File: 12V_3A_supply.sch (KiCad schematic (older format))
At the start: 14 parts, among them U1 TPS54561

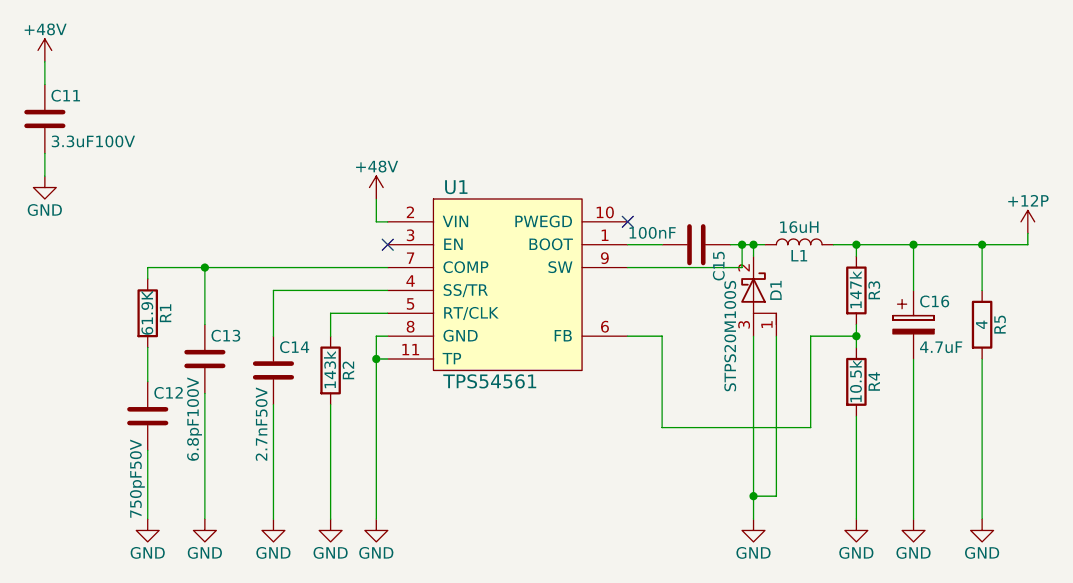
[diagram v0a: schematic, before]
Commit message: add MPN and change footprints
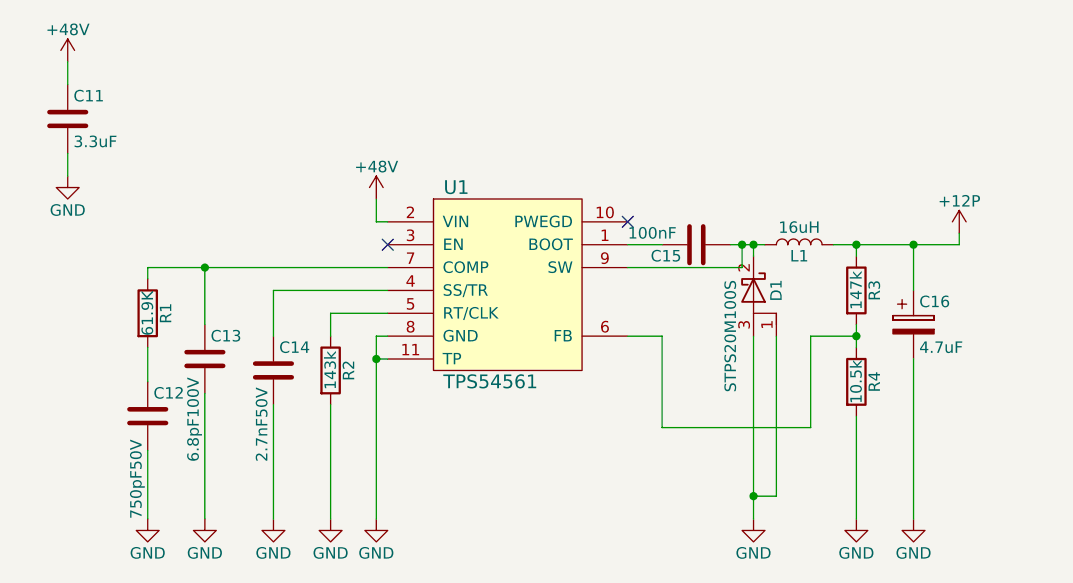
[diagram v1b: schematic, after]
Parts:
- removed R5: 4, Resistors_SMD:R_0402, symbol R
- C11: value 3.3uF100V -> 3.3uF; footprint Capacitors_SMD:C_1206 -> Capacitors_SMD:C_1210; MPN (none) -> 2211157
- C12: MPN (none) -> 1865436
- C13: MPN (none) -> 1865503
- C14: footprint Capacitors_SMD:C_0805 -> Capacitors_SMD:C_0603; MPN (none) -> 2680086
- C15: MPN (none) -> 2690952
- C16: footprint (none) -> Capacitor_SMD:CP_Elec_4x5.3; MPN (none) -> 2630483
- D1: MPN (none) -> 2325907
- L1: MPN (none) -> 2211625
- R1: MPN (none) -> 2073167
- R2: MPN (none) -> 2140944
- R3: MPN (none) -> 2302855
- R4: MPN (none) -> 1803138
- U1: MPN (none) -> TPS54561DPRT
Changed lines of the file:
@@
 LIBS:contrib
 LIBS:valves
+LIBS:MB_DEVICE
 LIBS:power_board-cache
 EELAYER 25 0
@@
 F 2 "MB_LIB:TPS54561" H 5450 3400 60  0001 C CNN
 F 3 "" H 5450 3400 60  0001 C CNN
+F 4 "TPS54561DPRT" H 5450 3400 60  0001 C CNN "MPN"
 	1    5450 3400
 	1    0    0    -1
@@
 Connection ~ 4900 3650
 $Comp
-L GND #PWR023
+L GND #PWR033
 U 1 1 5AA6E74F
 P 4900 4350
-F 0 "#PWR023" H 4900 4100 50  0001 C CNN
+F 0 "#PWR033" H 4900 4100 50  0001 C CNN
 F 1 "GND" H 4900 4200 50  0000 C CNN
 F 2 "" H 4900 4350 50  0001 C CNN
 F 3 "" H 4900 4350 50  0001 C CNN
 	1    4900 4350
-	1    0    0    -1
-$EndComp
-$Comp
-L C C11
-U 1 1 5AA6E768
-P 3450 2600
-F 0 "C11" H 3475 2700 50  0000 L CNN
-F 1 "3.3uF100V" H 3475 2500 50  0000 L CNN
-F 2 "Capacitors_SMD:C_1206" H 3488 2450 50  0001 C CNN
-F 3 "" H 3450 2600 50  0001 C CNN
-	1    3450 2600
 	1    0    0    -1
 $EndComp
@@
 F 2 "Capacitors_SMD:C_0402" H 3938 3750 50  0001 C CNN
 F 3 "" H 3900 3900 50  0001 C CNN
+F 4 "1865436" H 3900 3900 60  0001 C CNN "MPN"
 	1    3900 3900
-	1    0    0    -1
-$EndComp
-$Comp
-L C C13
-U 1 1 5AA6E7C6
-P 4150 3650
-F 0 "C13" H 4175 3750 50  0000 L CNN
-F 1 "6.8pF100V" V 4100 3200 50  0000 L CNN
-F 2 "Capacitors_SMD:C_0603" H 4188 3500 50  0001 C CNN
-F 3 "" H 4150 3650 50  0001 C CNN
-	1    4150 3650
-	1    0    0    -1
-$EndComp
-$Comp
-L C C14
-U 1 1 5AA6E7E8
-P 4450 3700
-F 0 "C14" H 4475 3800 50  0000 L CNN
-F 1 "2.7nF50V" V 4400 3300 50  0000 L CNN
-F 2 "Capacitors_SMD:C_0805" H 4488 3550 50  0001 C CNN
-F 3 "" H 4450 3700 50  0001 C CNN
-	1    4450 3700
 	1    0    0    -1
 $EndComp
@@
 F 2 "Resistors_SMD:R_0402" V 3830 3450 50  0001 C CNN
 F 3 "" H 3900 3450 50  0001 C CNN
+F 4 "2073167" V 3900 3450 60  0001 C CNN "MPN"
 	1    3900 3450
 	1    0    0    -1
@@
 F 2 "Resistors_SMD:R_0402" V 4630 3700 50  0001 C CNN
 F 3 "" H 4700 3700 50  0001 C CNN
+F 4 "2140944" V 4700 3700 60  0001 C CNN "MPN"
 	1    4700 3700
 	1    0    0    -1
-$EndComp
-$Comp
-L C C15
-U 1 1 5AA6E89F
-P 6300 3150
-F 0 "C15" H 6325 3250 50  0000 L CNN
-F 1 "100nF" V 6250 2850 50  0000 L CNN
-F 2 "Capacitors_SMD:C_0402" H 6338 3000 50  0001 C CNN
-F 3 "" H 6300 3150 50  0001 C CNN
-	1    6300 3150
-	0    1    1    0
 $EndComp
 $Comp
@@
 F 2 "Resistors_SMD:R_0402" V 6930 3350 50  0001 C CNN
 F 3 "" H 7000 3350 50  0001 C CNN
+F 4 "2302855" V 7000 3350 60  0001 C CNN "MPN"
 	1    7000 3350
 	1    0    0    -1
@@
 F 2 "Resistors_SMD:R_0402" V 6930 3750 50  0001 C CNN
 F 3 "" H 7000 3750 50  0001 C CNN
+F 4 "1803138" V 7000 3750 60  0001 C CNN "MPN"
 	1    7000 3750
 	1    0    0    -1
 $EndComp
 $Comp
-L +48V #PWR024
-U 1 1 5AA6EAEE
-P 3450 2350
-F 0 "#PWR024" H 3450 2200 50  0001 C CNN
-F 1 "+48V" H 3450 2490 50  0000 C CNN
-F 2 "" H 3450 2350 50  0001 C CNN
-F 3 "" H 3450 2350 50  0001 C CNN
-	1    3450 2350
-	1    0    0    -1
-$EndComp
-$Comp
-L +48V #PWR025
+L +48V #PWR034
 U 1 1 5AA6EB2F
 P 4900 2950
-F 0 "#PWR025" H 4900 2800 50  0001 C CNN
+F 0 "#PWR034" H 4900 2800 50  0001 C CNN
 F 1 "+48V" H 4900 3090 50  0000 C CNN
 F 2 "" H 4900 2950 50  0001 C CNN
@@
 	1    0    0    -1
 $EndComp
-$Comp
-L GND #PWR026
-U 1 1 5AA6EB62
-P 3450 2850
-F 0 "#PWR026" H 3450 2600 50  0001 C CNN
-F 1 "GND" H 3450 2700 50  0000 C CNN
-F 2 "" H 3450 2850 50  0001 C CNN
-F 3 "" H 3450 2850 50  0001 C CNN
-	1    3450 2850
-	1    0    0    -1
-$EndComp
 Wire Wire Line
 	4900 2950 4900 3050
 Wire Wire Line
 	4900 3050 4950 3050
-Wire Wire Line
-	3450 2850 3450 2750
-Wire Wire Line
-	3450 2450 3450 2350
 Wire Wire Line
 	4150 3500 4150 3250
@@
 	3900 4050 3900 4350
 Wire Wire Line
-	4150 3800 4150 4350
-Wire Wire Line
 	4450 3850 4450 4350
 Wire Wire Line
 	4700 3850 4700 4350
 $Comp
-L GND #PWR027
+L GND #PWR035
 U 1 1 5AA6EECF
 P 4700 4350
-F 0 "#PWR027" H 4700 4100 50  0001 C CNN
+F 0 "#PWR035" H 4700 4100 50  0001 C CNN
 F 1 "GND" H 4700 4200 50  0000 C CNN
 F 2 "" H 4700 4350 50  0001 C CNN
@@
 $EndComp
 $Comp
-L GND #PWR028
+L GND #PWR036
 U 1 1 5AA6EEF8
 P 4450 4350
-F 0 "#PWR028" H 4450 4100 50  0001 C CNN
+F 0 "#PWR036" H 4450 4100 50  0001 C CNN
 F 1 "GND" H 4450 4200 50  0000 C CNN
 F 2 "" H 4450 4350 50  0001 C CNN
@@
 $EndComp
 $Comp
-L GND #PWR029
+L GND #PWR037
 U 1 1 5AA6EF21
 P 4150 4350
-F 0 "#PWR029" H 4150 4100 50  0001 C CNN
+F 0 "#PWR037" H 4150 4100 50  0001 C CNN
 F 1 "GND" H 4150 4200 50  0000 C CNN
 F 2 "" H 4150 4350 50  0001 C CNN
@@
 $EndComp
 $Comp
-L GND #PWR030
+L GND #PWR038
 U 1 1 5AA6EF4A
 P 3900 4350
-F 0 "#PWR030" H 3900 4100 50  0001 C CNN
+F 0 "#PWR038" H 3900 4100 50  0001 C CNN
 F 1 "GND" H 3900 4200 50  0000 C CNN
 F 2 "" H 3900 4350 50  0001 C CNN
@@
 F 2 "Inductors_SMD:L_Wuerth_HCI-1050" H 6750 3150 50  0001 C CNN
 F 3 "http://katalog.we-online.de/pbs/datasheet/7443251600.pdf" H 6750 3150 50  0001 C CNN
+F 4 "2211625" V 6750 3150 60  0001 C CNN "MPN"
 	1    6750 3150
 	0    -1   -1   0
@@
 F 0 "C16" H 7275 3600 50  0000 L CNN
 F 1 "4.7uF" H 7275 3400 50  0000 L CNN
-F 2 "" H 7288 3350 50  0001 C CNN
+F 2 "Capacitor_SMD:CP_Elec_4x5.3" H 7288 3350 50  0001 C CNN
 F 3 "" H 7250 3500 50  0001 C CNN
+F 4 "2630483" H 7250 3500 60  0001 C CNN "MPN"
 	1    7250 3500
 	1    0    0    -1
@@
 Connection ~ 7000 3150
 Wire Wire Line
-	6900 3150 7750 3150
+	6900 3150 7450 3150
 Wire Wire Line
 	7250 3150 7250 3350
 Wire Wire Line
 	7250 3650 7250 4350
-$Comp
-L R R5
-U 1 1 5AA6F613
-P 7550 3500
-F 0 "R5" V 7630 3500 50  0000 C CNN
-F 1 "4" V 7550 3500 50  0000 C CNN
-F 2 "Resistors_SMD:R_0402" V 7480 3500 50  0001 C CNN
-F 3 "" H 7550 3500 50  0001 C CNN
-	1    7550 3500
-	1    0    0    -1
-$EndComp
-Wire Wire Line
-	7550 3150 7550 3350
 Connection ~ 7250 3150
-Wire Wire Line
-	7550 3650 7550 4350
 Wire Wire Line
 	6000 3250 6500 3250
@@
 Connection ~ 6550 3150
 $Comp
-L GND #PWR031
+L GND #PWR039
 U 1 1 5AA6F863
 P 6550 4350
-F 0 "#PWR031" H 6550 4100 50  0001 C CNN
+F 0 "#PWR039" H 6550 4100 50  0001 C CNN
 F 1 "GND" H 6550 4200 50  0000 C CNN
 F 2 "" H 6550 4350 50  0001 C CNN
@@
 	7000 3900 7000 4350
 $Comp
-L GND #PWR032
+L GND #PWR040
 U 1 1 5AA6F9CD
 P 7000 4350
-F 0 "#PWR032" H 7000 4100 50  0001 C CNN
+F 0 "#PWR040" H 7000 4100 50  0001 C CNN
 F 1 "GND" H 7000 4200 50  0000 C CNN
 F 2 "" H 7000 4350 50  0001 C CNN
@@
 $EndComp
 $Comp
-L GND #PWR033
+L GND #PWR041
 U 1 1 5AA6FA05
 P 7250 4350
-F 0 "#PWR033" H 7250 4100 50  0001 C CNN
+F 0 "#PWR041" H 7250 4100 50  0001 C CNN
 F 1 "GND" H 7250 4200 50  0000 C CNN
 F 2 "" H 7250 4350 50  0001 C CNN
@@
 	1    0    0    -1
 $EndComp
-$Comp
-L GND #PWR034
-U 1 1 5AA6FA3D
-P 7550 4350
-F 0 "#PWR034" H 7550 4100 50  0001 C CNN
-F 1 "GND" H 7550 4200 50  0000 C CNN
-F 2 "" H 7550 4350 50  0001 C CNN
-F 3 "" H 7550 4350 50  0001 C CNN
-	1    7550 4350
-	1    0    0    -1
-$EndComp
-Wire Wire Line
-	7750 3150 7750 3100
-Connection ~ 7550 3150
+Wire Wire Line
+	7450 3150 7450 3100
 $Comp
 L D_Schottky_AKA D1
@@
 F 2 "TO_SOT_Packages_SMD:TO-263-2" H 6550 3350 50  0001 C CNN
 F 3 "http://www.st.com/content/ccc/resource/technical/document/datasheet/group2/8f/d3/41/ea/82/b2/4b/5a/CD00228904/files/CD00228904.pdf/jcr:content/translations/en.CD00228904.pdf" H 6550 3350 50  0001 C CNN
+F 4 "2325907" H 6550 3350 60  0001 C CNN "MPN"
 	1    6550 3350
 	0    1    1    0
@@
 NoConn ~ 6000 3050
 $Comp
-L +12P #PWR035
+L +12P #PWR042
 U 1 1 5AA81E40
-P 7750 3100
-F 0 "#PWR035" H 7750 2950 50  0001 C CNN
-F 1 "+12P" H 7750 3240 50  0000 C CNN
-F 2 "" H 7750 3100 50  0001 C CNN
-F 3 "" H 7750 3100 50  0001 C CNN
-	1    7750 3100
-	1    0    0    -1
-$EndComp
+P 7450 3100
+F 0 "#PWR042" H 7450 2950 50  0001 C CNN
+F 1 "+12P" H 7450 3240 50  0000 C CNN
+F 2 "" H 7450 3100 50  0001 C CNN
+F 3 "" H 7450 3100 50  0001 C CNN
+	1    7450 3100
+	1    0    0    -1
+$EndComp
+$Comp
+L C C11
+U 1 1 5AB03638
+P 3550 2600
+F 0 "C11" H 3575 2700 50  0000 L CNN
+F 1 "3.3uF" H 3575 2500 50  0000 L CNN
+F 2 "Capacitors_SMD:C_1210" H 3588 2450 50  0001 C CNN
+F 3 "" H 3550 2600 50  0001 C CNN
+F 4 "2211157" H 3550 2600 60  0001 C CNN "MPN"
+	1    3550 2600
+	1    0    0    -1
+$EndComp
+$Comp
+L +48V #PWR043
+U 1 1 5AB0363F
+P 3550 2350
+F 0 "#PWR043" H 3550 2200 50  0001 C CNN
+F 1 "+48V" H 3550 2490 50  0000 C CNN
+F 2 "" H 3550 2350 50  0001 C CNN
+F 3 "" H 3550 2350 50  0001 C CNN
+	1    3550 2350
+	1    0    0    -1
+$EndComp
+$Comp
+L GND #PWR044
+U 1 1 5AB03645
+P 3550 2850
+F 0 "#PWR044" H 3550 2600 50  0001 C CNN
+F 1 "GND" H 3550 2700 50  0000 C CNN
+F 2 "" H 3550 2850 50  0001 C CNN
+F 3 "" H 3550 2850 50  0001 C CNN
+	1    3550 2850
+	1    0    0    -1
+$EndComp
+Wire Wire Line
+	3550 2850 3550 2750
+Wire Wire Line
+	3550 2450 3550 2350
+$Comp
+L C C15
+U 1 1 5AB03980
+P 6300 3150
+F 0 "C15" V 6350 2950 50  0000 L CNN
+F 1 "100nF" V 6250 2850 50  0000 L CNN
+F 2 "Capacitors_SMD:C_0402" H 6338 3000 50  0001 C CNN
+F 3 "" H 6300 3150 50  0001 C CNN
+F 4 "2690952" H 6300 3150 60  0001 C CNN "MPN"
+	1    6300 3150
+	0    1    1    0
+$EndComp
+$Comp
+L C C13
+U 1 1 5AB03E47
+P 4150 3650
+F 0 "C13" H 4175 3750 50  0000 L CNN
+F 1 "6.8pF100V" V 4100 3200 50  0000 L CNN
+F 2 "Capacitors_SMD:C_0603" H 4188 3500 50  0001 C CNN
+F 3 "" H 4150 3650 50  0001 C CNN
+F 4 "1865503" H 4150 3650 60  0001 C CNN "MPN"
+	1    4150 3650
+	1    0    0    -1
+$EndComp
+$Comp
+L C C14
+U 1 1 5AB03E4F
+P 4450 3700
+F 0 "C14" H 4475 3800 50  0000 L CNN
+F 1 "2.7nF50V" V 4400 3300 50  0000 L CNN
+F 2 "Capacitors_SMD:C_0603" H 4488 3550 50  0001 C CNN
+F 3 "" H 4450 3700 50  0001 C CNN
+F 4 "2680086" H 4450 3700 60  0001 C CNN "MPN"
+	1    4450 3700
+	1    0    0    -1
+$EndComp
+Wire Wire Line
+	4150 3800 4150 4350
 $EndSCHEMATC

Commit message: mpn was changed
added needed conectors
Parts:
- C11: MPN 2211157 -> CGA6P3X7R1H335K250AB
- C12: MPN 1865436 -> C0402C751J5GACTU
- C13: MPN 1865503 -> C0603C689C1GACTU
- C14: MPN 2680086 -> C0603C272J5RACTU
- C15: MPN 2690952 -> 04025C104KAT2A
- C16: MPN 2630483 -> MCVVT016M4R7CA1L
- D1: MPN 2325907 -> STPS20M100SG-TR
- L1: MPN 2211625 -> 7443251600
- R1: MPN 2073167 -> MCMR04X6192FTL
- R2: MPN 2140944 -> CRCW0402143KFKED
- R3: MPN 2302855 -> ERJ2RKF1473X
- R4: MPN 1803138 -> MC00625W0402110K5
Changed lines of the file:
@@
 F 2 "Capacitors_SMD:C_0402" H 3938 3750 50  0001 C CNN
 F 3 "" H 3900 3900 50  0001 C CNN
-F 4 "1865436" H 3900 3900 60  0001 C CNN "MPN"
+F 4 "C0402C751J5GACTU" H 3900 3900 60  0001 C CNN "MPN"
 	1    3900 3900
 	1    0    0    -1
@@
 F 2 "Resistors_SMD:R_0402" V 3830 3450 50  0001 C CNN
 F 3 "" H 3900 3450 50  0001 C CNN
-F 4 "2073167" V 3900 3450 60  0001 C CNN "MPN"
+F 4 "MCMR04X6192FTL" V 3900 3450 60  0001 C CNN "MPN"
 	1    3900 3450
 	1    0    0    -1
@@
 F 2 "Resistors_SMD:R_0402" V 4630 3700 50  0001 C CNN
 F 3 "" H 4700 3700 50  0001 C CNN
-F 4 "2140944" V 4700 3700 60  0001 C CNN "MPN"
+F 4 "CRCW0402143KFKED" V 4700 3700 60  0001 C CNN "MPN"
 	1    4700 3700
 	1    0    0    -1
@@
 F 2 "Resistors_SMD:R_0402" V 6930 3350 50  0001 C CNN
 F 3 "" H 7000 3350 50  0001 C CNN
-F 4 "2302855" V 7000 3350 60  0001 C CNN "MPN"
+F 4 "ERJ2RKF1473X" V 7000 3350 60  0001 C CNN "MPN"
 	1    7000 3350
 	1    0    0    -1
@@
 F 2 "Resistors_SMD:R_0402" V 6930 3750 50  0001 C CNN
 F 3 "" H 7000 3750 50  0001 C CNN
-F 4 "1803138" V 7000 3750 60  0001 C CNN "MPN"
+F 4 "MC00625W0402110K5" V 7000 3750 60  0001 C CNN "MPN"
 	1    7000 3750
 	1    0    0    -1
@@
 F 2 "Inductors_SMD:L_Wuerth_HCI-1050" H 6750 3150 50  0001 C CNN
 F 3 "http://katalog.we-online.de/pbs/datasheet/7443251600.pdf" H 6750 3150 50  0001 C CNN
-F 4 "2211625" V 6750 3150 60  0001 C CNN "MPN"
+F 4 "7443251600" V 6750 3150 60  0001 C CNN "MPN"
 	1    6750 3150
 	0    -1   -1   0
@@
 F 2 "Capacitor_SMD:CP_Elec_4x5.3" H 7288 3350 50  0001 C CNN
 F 3 "" H 7250 3500 50  0001 C CNN
-F 4 "2630483" H 7250 3500 60  0001 C CNN "MPN"
+F 4 "MCVVT016M4R7CA1L" H 7250 3500 60  0001 C CNN "MPN"
 	1    7250 3500
 	1    0    0    -1
@@
 F 2 "TO_SOT_Packages_SMD:TO-263-2" H 6550 3350 50  0001 C CNN
 F 3 "http://www.st.com/content/ccc/resource/technical/document/datasheet/group2/8f/d3/41/ea/82/b2/4b/5a/CD00228904/files/CD00228904.pdf/jcr:content/translations/en.CD00228904.pdf" H 6550 3350 50  0001 C CNN
-F 4 "2325907" H 6550 3350 60  0001 C CNN "MPN"
+F 4 "STPS20M100SG-TR" H 6550 3350 60  0001 C CNN "MPN"
 	1    6550 3350
 	0    1    1    0
@@
 F 2 "Capacitors_SMD:C_1210" H 3588 2450 50  0001 C CNN
 F 3 "" H 3550 2600 50  0001 C CNN
-F 4 "2211157" H 3550 2600 60  0001 C CNN "MPN"
+F 4 "CGA6P3X7R1H335K250AB" H 3550 2600 60  0001 C CNN "MPN"
 	1    3550 2600
 	1    0    0    -1
@@
 F 2 "Capacitors_SMD:C_0402" H 6338 3000 50  0001 C CNN
 F 3 "" H 6300 3150 50  0001 C CNN
-F 4 "2690952" H 6300 3150 60  0001 C CNN "MPN"
+F 4 "04025C104KAT2A" H 6300 3150 60  0001 C CNN "MPN"
 	1    6300 3150
 	0    1    1    0
@@
 F 2 "Capacitors_SMD:C_0603" H 4188 3500 50  0001 C CNN
 F 3 "" H 4150 3650 50  0001 C CNN
-F 4 "1865503" H 4150 3650 60  0001 C CNN "MPN"
+F 4 "C0603C689C1GACTU" H 4150 3650 60  0001 C CNN "MPN"
 	1    4150 3650
 	1    0    0    -1
@@
 F 2 "Capacitors_SMD:C_0603" H 4488 3550 50  0001 C CNN
 F 3 "" H 4450 3700 50  0001 C CNN
-F 4 "2680086" H 4450 3700 60  0001 C CNN "MPN"
+F 4 "C0603C272J5RACTU" H 4450 3700 60  0001 C CNN "MPN"
 	1    4450 3700
 	1    0    0    -1

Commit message: kicost file added
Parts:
- C16: MPN MCVVT016M4R7CA1L -> EEE-1CA4R7NR
- R1: MPN MCMR04X6192FTL -> RMCF0402FT61K9CT-ND
- R4: MPN MC00625W0402110K5 -> RC0402FR-0710K5L
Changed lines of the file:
@@
 LIBS:contrib
 LIBS:valves
-LIBS:MB_DEVICE
 LIBS:power_board-cache
 EELAYER 25 0
@@
 F 2 "Resistors_SMD:R_0402" V 3830 3450 50  0001 C CNN
 F 3 "" H 3900 3450 50  0001 C CNN
-F 4 "MCMR04X6192FTL" V 3900 3450 60  0001 C CNN "MPN"
+F 4 "RMCF0402FT61K9CT-ND " V 3900 3450 60  0001 C CNN "MPN"
 	1    3900 3450
 	1    0    0    -1
@@
 F 2 "Resistors_SMD:R_0402" V 6930 3750 50  0001 C CNN
 F 3 "" H 7000 3750 50  0001 C CNN
-F 4 "MC00625W0402110K5" V 7000 3750 60  0001 C CNN "MPN"
+F 4 "RC0402FR-0710K5L " V 7000 3750 60  0001 C CNN "MPN"
 	1    7000 3750
 	1    0    0    -1
@@
 F 2 "Capacitor_SMD:CP_Elec_4x5.3" H 7288 3350 50  0001 C CNN
 F 3 "" H 7250 3500 50  0001 C CNN
-F 4 "MCVVT016M4R7CA1L" H 7250 3500 60  0001 C CNN "MPN"
+F 4 "EEE-1CA4R7NR " H 7250 3500 60  0001 C CNN "MPN"
 	1    7250 3500
 	1    0    0    -1
